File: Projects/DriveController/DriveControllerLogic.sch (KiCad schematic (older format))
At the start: 37 parts, among them J1 HPCE_40-24, J2 ISP_Header, U1 ATMega32M1, U2 MCP2562, U3 ATA6844, U4 ACS710

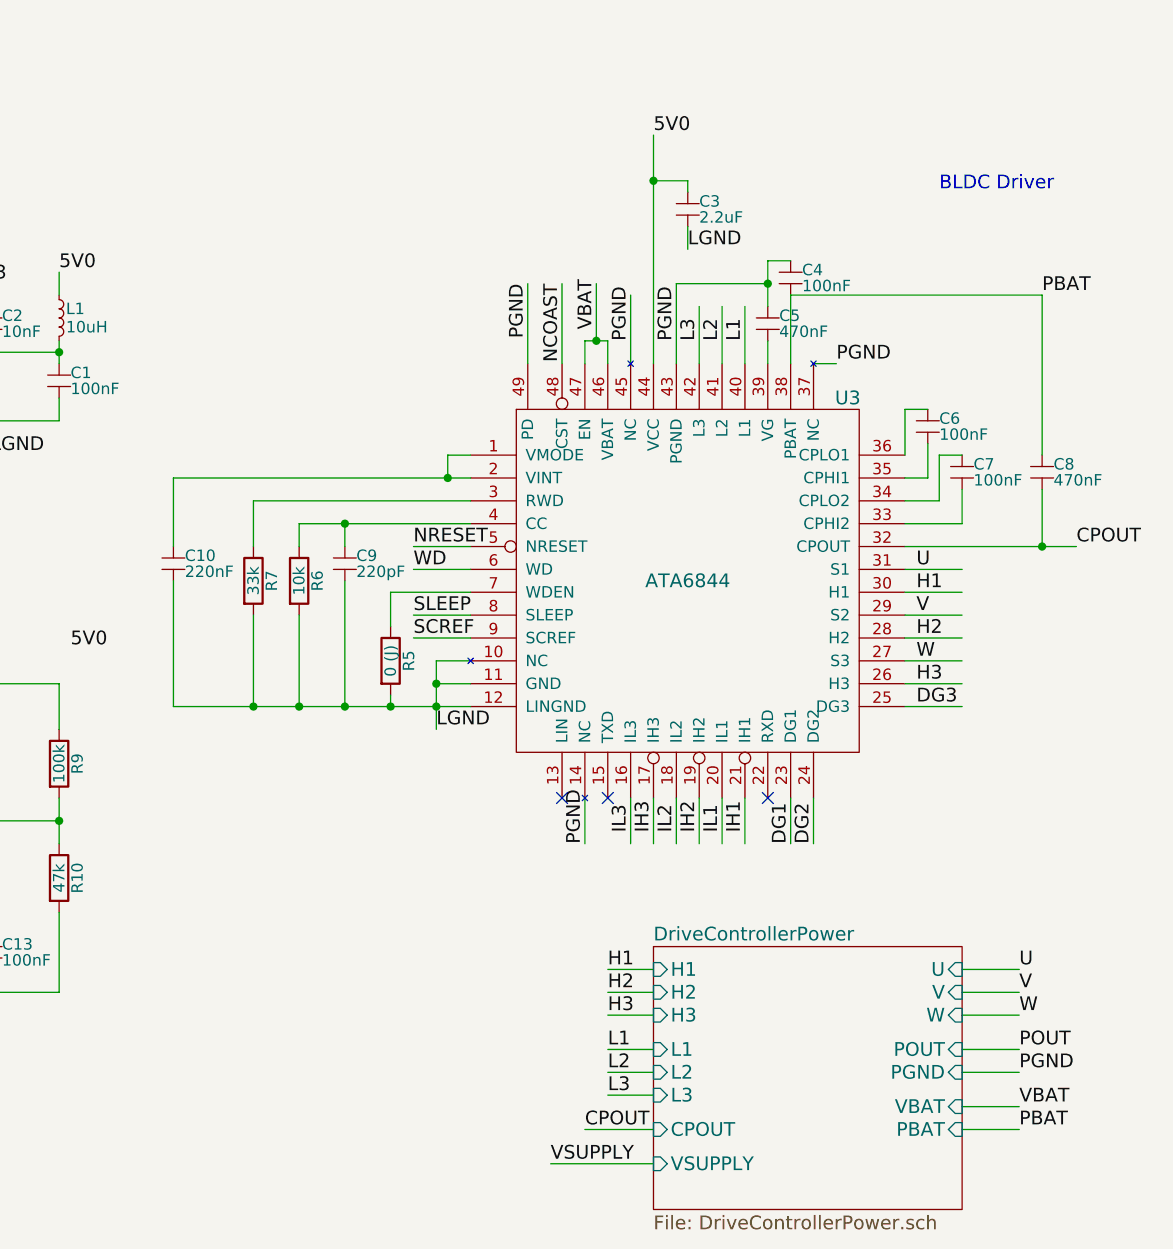
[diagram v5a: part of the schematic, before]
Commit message: Added reference designs, work on Pi Board and (deprecated) motor control board
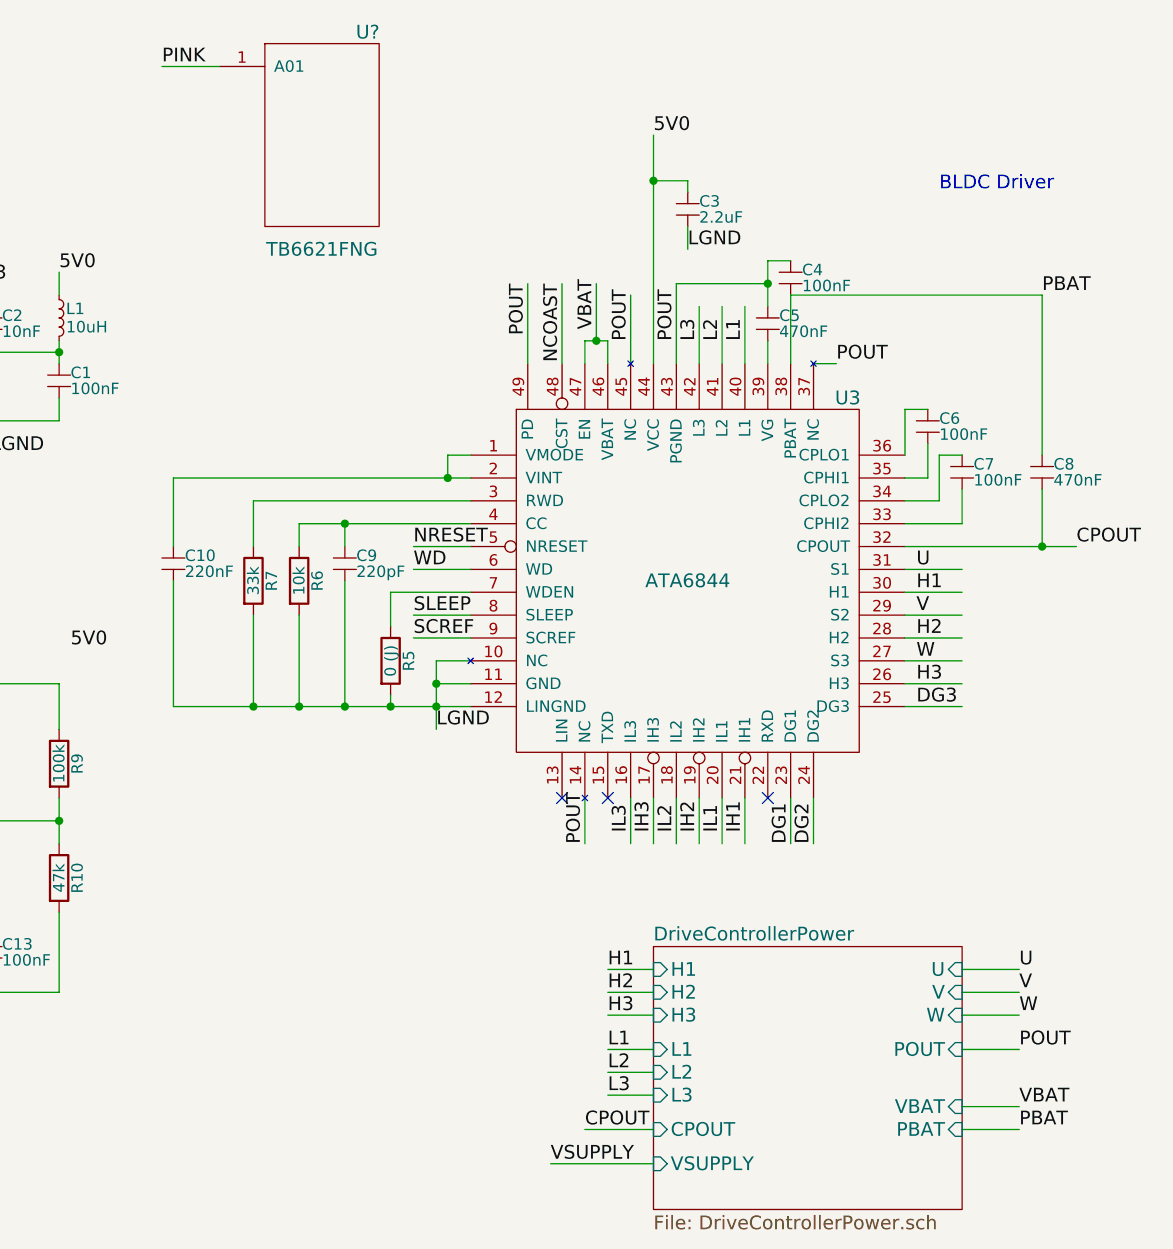
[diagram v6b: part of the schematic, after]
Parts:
- added U?: TB6621FNG, symbol TB6621FNG
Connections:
- net labels added: PINK
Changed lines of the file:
@@
 LGND
 Text Label 8450 2000 1    60   ~ 0
-PGND
+POUT
 Text Label 8650 2000 1    60   ~ 0
-PGND
+POUT
 Text Label 8750 2000 1    60   ~ 0
 L3
@@
 $EndComp
 Text Label 9350 2100 0    60   ~ 0
-PGND
+POUT
 Text Label 9700 3000 0    60   ~ 0
 U
@@
 IL3
 Text Label 8250 4200 1    60   ~ 0
-PGND
+POUT
 Text Label 7600 3700 0    60   ~ 0
 LGND
@@
 Text Label 10150 5100 0    60   ~ 0
 POUT
-Text Label 10150 5200 0    60   ~ 0
-PGND
 Text Label 10150 5350 0    60   ~ 0
 VBAT
@@
 Text Label 4800 2550 0    60   ~ 0
 5V0
-$Sheet
-S 8550 4650 1350 1150
-U 56465186
-F0 "DriveControllerPower" 60
-F1 "DriveControllerPower.sch" 60
-F2 "U" I R 9900 4750 60
-F3 "V" I R 9900 4850 60
-F4 "W" I R 9900 4950 60
-F5 "POUT" I R 9900 5100 60
-F6 "PGND" I R 9900 5200 60
-F7 "VBAT" I R 9900 5350 60
-F8 "PBAT" I R 9900 5450 60
-F9 "H1" I L 8550 4750 60
-F10 "H2" I L 8550 4850 60
-F11 "H3" I L 8550 4950 60
-F12 "L1" I L 8550 5100 60
-F13 "L2" I L 8550 5200 60
-F14 "L3" I L 8550 5300 60
-F15 "CPOUT" I L 8550 5450 60
-F16 "VSUPPLY" I L 8550 5600 60
-$EndSheet
 Text Label 10400 2900 0    60   ~ 0
 CPOUT
@@
 	9900 5100 10150 5100
 Wire Wire Line
-	9900 5200 10150 5200
-Wire Wire Line
 	9900 5350 10150 5350
 Wire Wire Line
@@
 	8000 1750 8000 2100
 Text Label 8000 1750 3    60   ~ 0
-PGND
+POUT
+$Sheet
+S 8550 4650 1350 1150
+U 56465186
+F0 "DriveControllerPower" 60
+F1 "DriveControllerPower.sch" 60
+F2 "U" I R 9900 4750 60
+F3 "V" I R 9900 4850 60
+F4 "W" I R 9900 4950 60
+F5 "POUT" I R 9900 5100 60
+F6 "VBAT" I R 9900 5350 60
+F7 "PBAT" I R 9900 5450 60
+F8 "H1" I L 8550 4750 60
+F9 "H2" I L 8550 4850 60
+F10 "H3" I L 8550 4950 60
+F11 "L1" I L 8550 5100 60
+F12 "L2" I L 8550 5200 60
+F13 "L3" I L 8550 5300 60
+F14 "CPOUT" I L 8550 5450 60
+F15 "VSUPPLY" I L 8550 5600 60
+$EndSheet
+$Comp
+L TB6621FNG U?
+U 1 1 56579FBD
+P 7100 1100
+F 0 "U?" H 7300 1550 60  0000 C CNN
+F 1 "TB6621FNG" H 7100 600 60  0000 C CNN
+F 2 "" H 7800 1500 60  0000 C CNN
+F 3 "" H 7800 1500 60  0000 C CNN
+	1    7100 1100
+	1    0    0    -1
+$EndComp
+Wire Wire Line
+	6650 800  6400 800
+Text Label 6400 800  0    60   ~ 0
+PINK
 $EndSCHEMATC
